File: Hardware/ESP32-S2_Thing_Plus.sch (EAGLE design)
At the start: 66 parts, among them J3 QWIIC_RA, J5 USB-C, J6 JTAG, Q1 2.5A/30V, Q2 MBT3904DW1T1, U1 ESP32-S2-WROOM, U2 CP210X, U3 AP2112, U4 MCP73831, U5 TC7USB40MU, Y1 32.768kHz

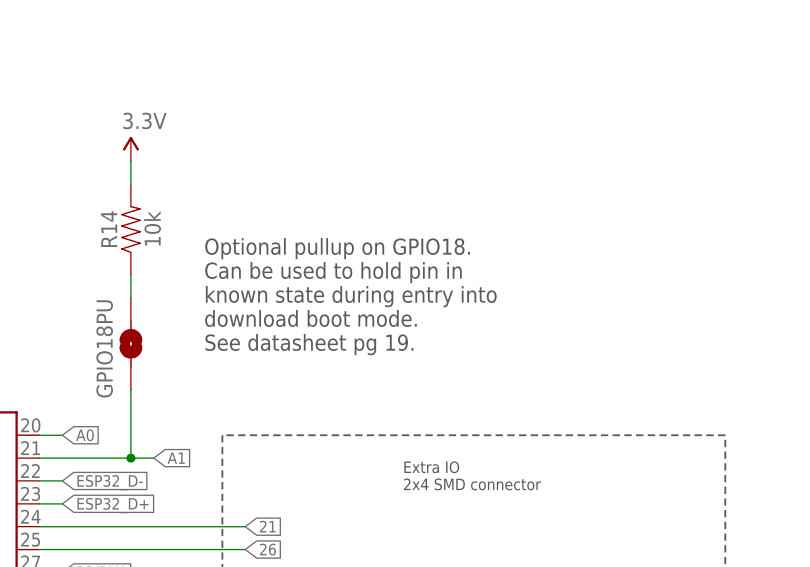
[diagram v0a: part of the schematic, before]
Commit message: Clarifying which datasheet to reference about GPIO18 pullup
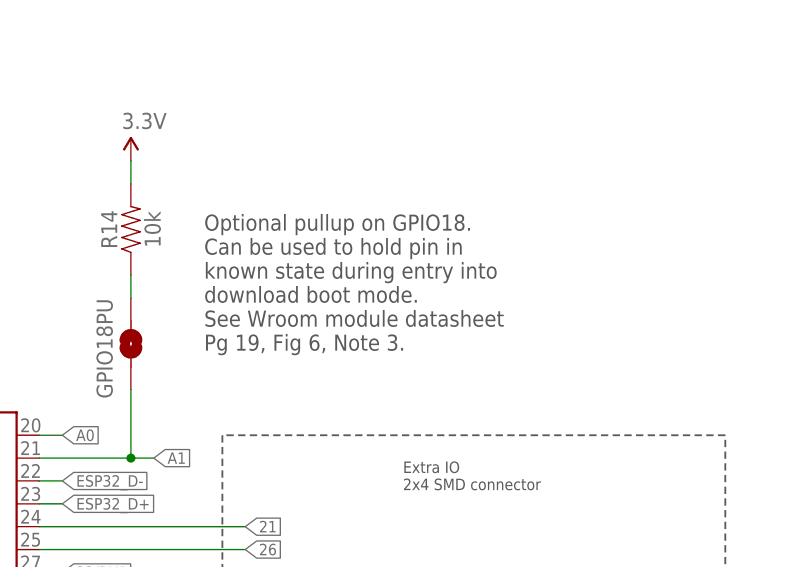
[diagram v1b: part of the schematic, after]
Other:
- note added: "Optional pullup on GPIO18. Can be used to hold pin in known state during entry into download boot mode. See Wroom module datasheet Pg 19, Fig 6, Note 3."
- note removed: "Optional pullup on GPIO18. Can be used to hold pin in known state during entry into download boot mode. See datasheet pg 19."
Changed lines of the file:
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@@
 known state during entry into
 download boot mode.
-See datasheet pg 19.</text>
+See Wroom module datasheet
+Pg 19, Fig 6, Note 3.</text>
 </plain>
 <instances>

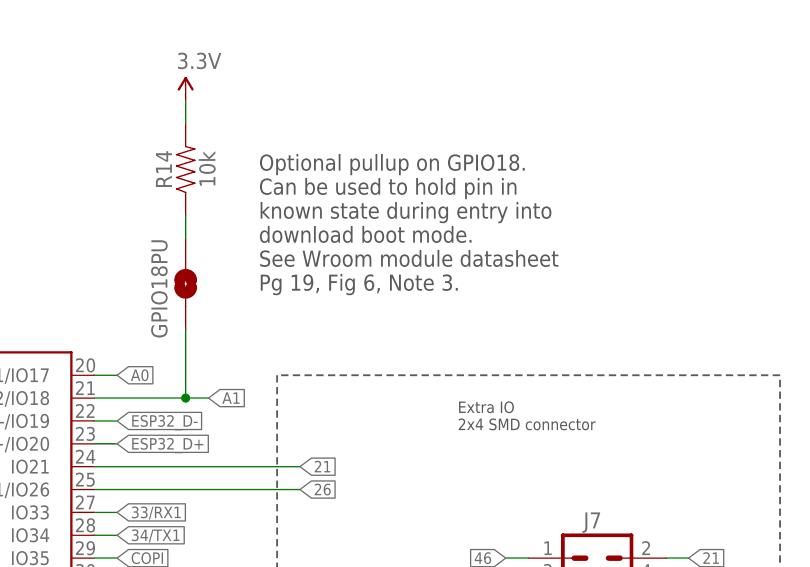
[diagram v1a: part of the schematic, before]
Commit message: GPIO18 paragraph DS page correction (PG 20)
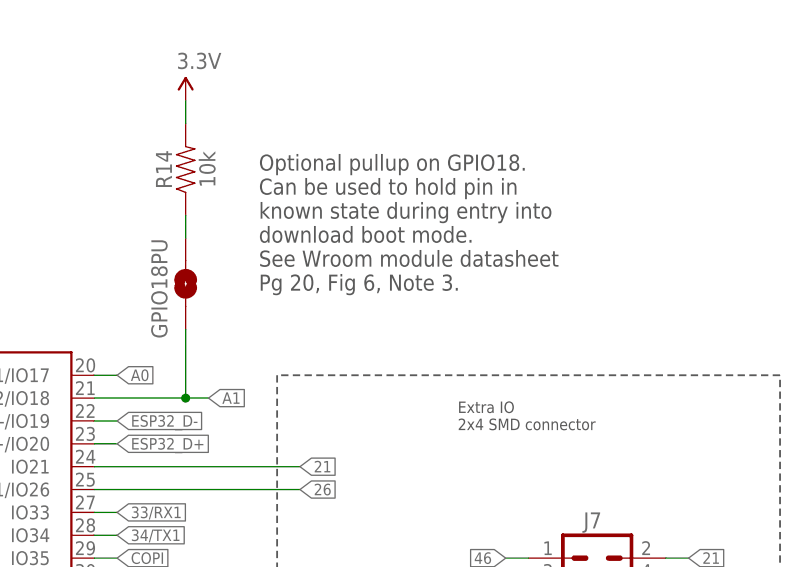
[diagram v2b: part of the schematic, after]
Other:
- note added: "Optional pullup on GPIO18. Can be used to hold pin in known state during entry into download boot mode. See Wroom module datasheet Pg 20, Fig 6, Note 3."
- note removed: "Optional pullup on GPIO18. Can be used to hold pin in known state during entry into download boot mode. See Wroom module datasheet Pg 19, Fig 6, Note 3."
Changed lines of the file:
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@@
 download boot mode.
 See Wroom module datasheet
-Pg 19, Fig 6, Note 3.</text>
+Pg 20, Fig 6, Note 3.</text>
 </plain>
 <instances>
